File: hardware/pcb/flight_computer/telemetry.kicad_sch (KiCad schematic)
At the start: 1 part, among them J1 NRF24L01

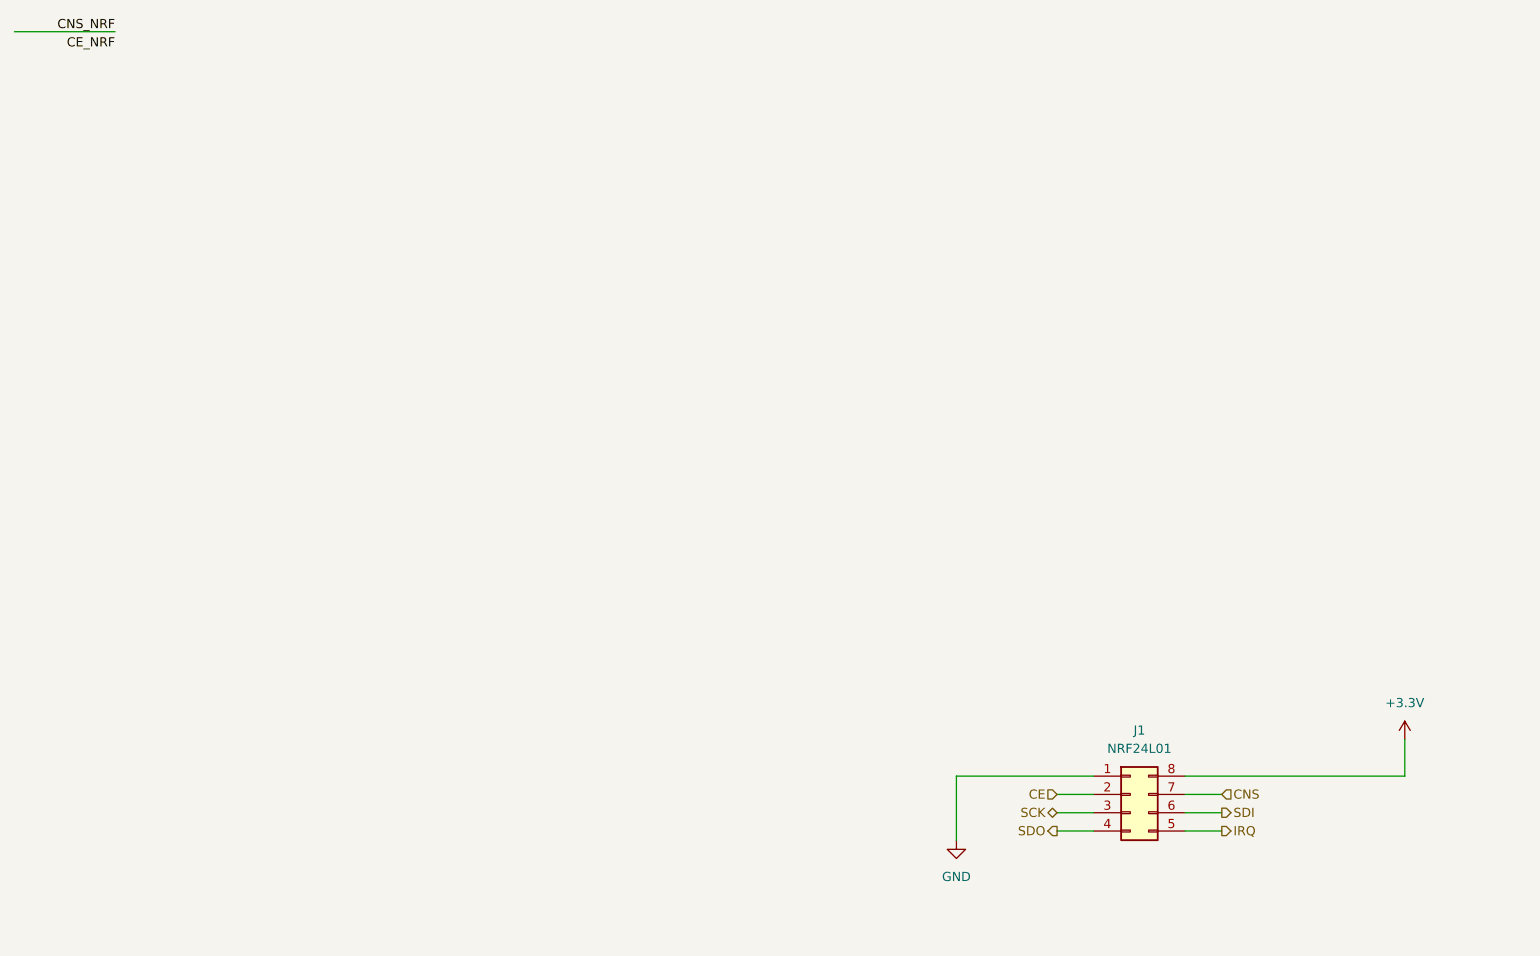
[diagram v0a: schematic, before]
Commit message: Added 3D model
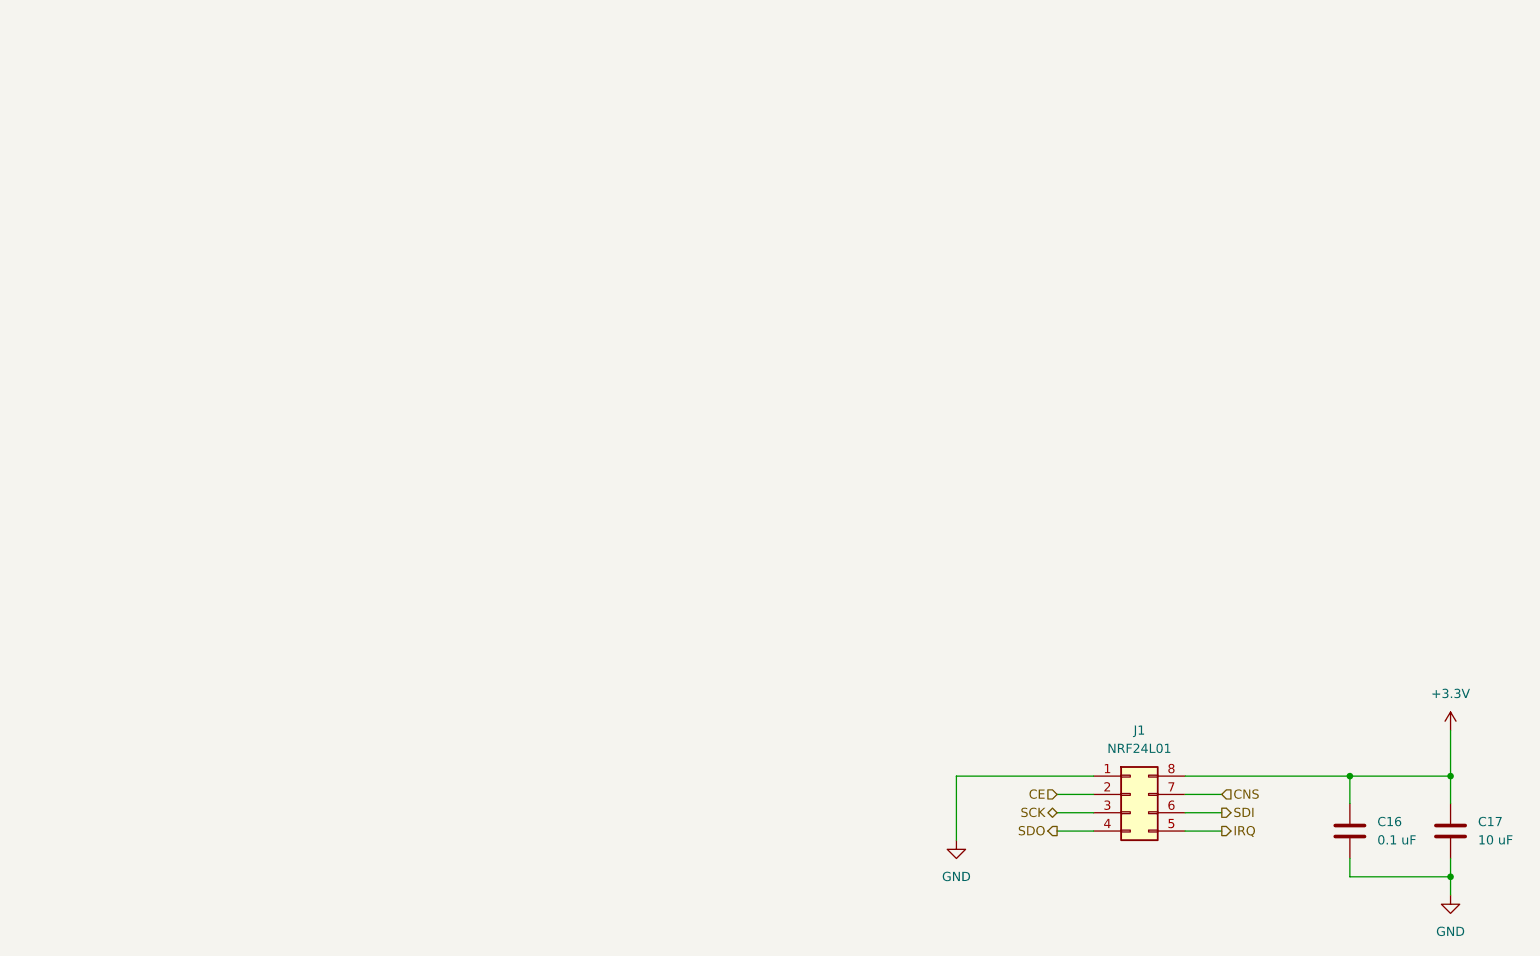
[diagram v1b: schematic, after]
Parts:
- added C16: 0.1 uF, Capacitor_SMD:C_0603_1608Metric, symbol Device:C
- added C17: 10 uF, Capacitor_SMD:C_0603_1608Metric, symbol Device:C
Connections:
- net +3.3V: now also C16.1, C17.1
- net GND: now also C16.2, C17.2
